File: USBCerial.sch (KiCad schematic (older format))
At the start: 3 parts, among them J1 USB_C, U1 CH340C

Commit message: First schematic complete using the CH340C
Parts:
- removed C1: 0.1uF, Capacitor_SMD:C_0603_1608Metric, symbol Device:C
- added C1, C2: 0.1uF 50V, Capacitor_SMD:C_0603_1608Metric_Pad1.08x0.95mm_HandSolder, symbol Device:C_Small
- added C3, C4: 1uF 50V, Capacitor_SMD:C_0603_1608Metric_Pad1.08x0.95mm_HandSolder, symbol Device:C_Small
- added JP1: Jumper, Connector_PinHeader_2.54mm:PinHeader_1x03_P2.54mm_Vertical, symbol Jumper:Jumper_3_Bridged12
- added U2: XC6206P332MR, Package_TO_SOT_SMD:SOT-23, symbol Regulator_Linear:XC6206PxxxMR
- U1: symbol Interface_USB:CH340C -> USBCerial:CH340C
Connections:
- net labels added: +3.3V, CTS, DTR, GNDD, RTS, RXD, TXD, VCC
- net labels removed: GND
- wire segments 12 -> 47
- no-connect marks 0 -> 6

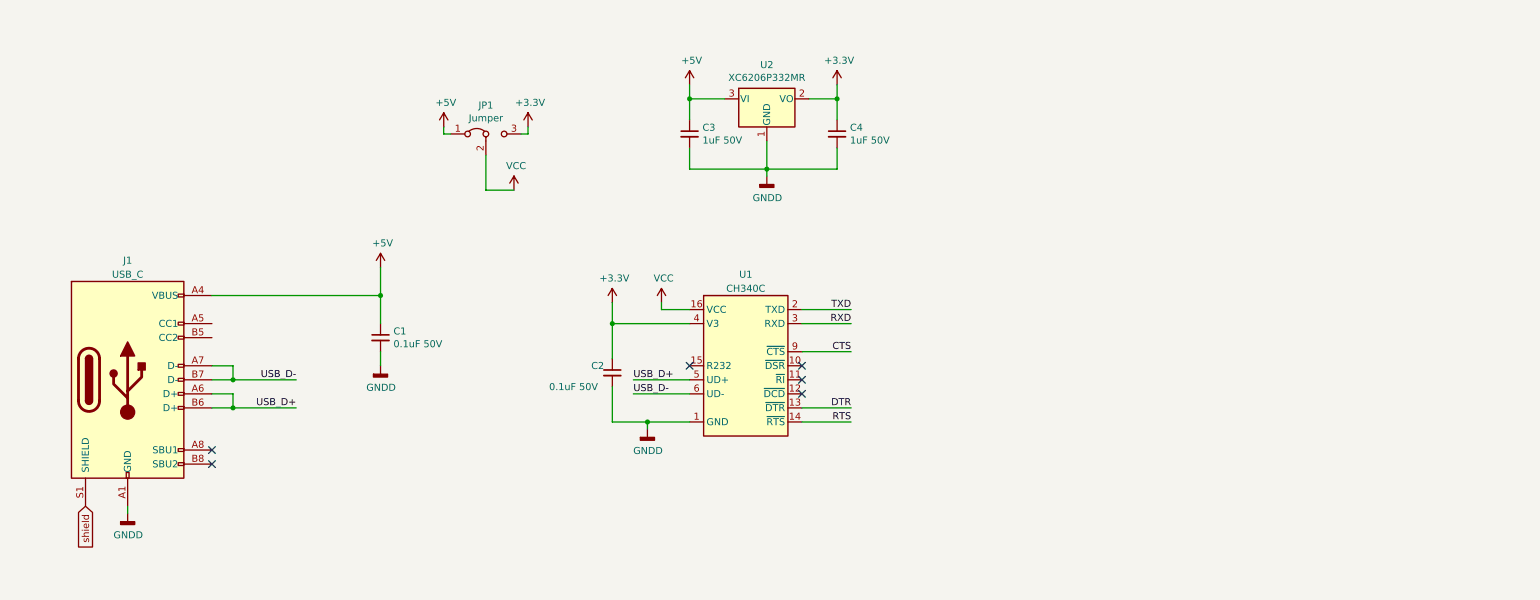
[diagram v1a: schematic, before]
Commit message: Complete schematic, Begin on PCB placment and design
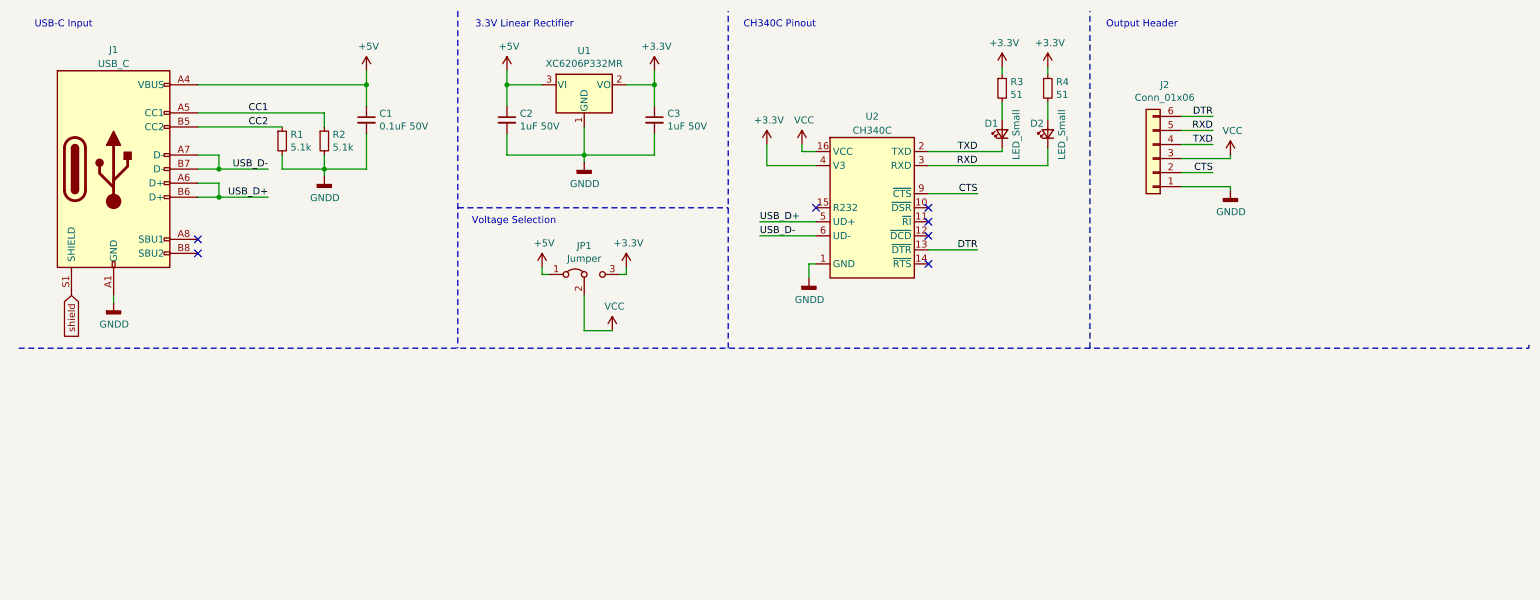
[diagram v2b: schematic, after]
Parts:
- removed C2: 0.1uF 50V, Capacitor_SMD:C_0603_1608Metric_Pad1.08x0.95mm_HandSolder, symbol Device:C_Small
- added D1, D2: LED_Small, LED_SMD:LED_0603_1608Metric_Castellated, symbol Device:LED_Small
- added J2: Conn_01x06, Connector_PinHeader_2.54mm:PinHeader_1x06_P2.54mm_Horizontal, symbol Connector_Generic:Conn_01x06
- added R1, R2: 5.1k, Resistor_SMD:R_0603_1608Metric_Pad0.98x0.95mm_HandSolder, symbol Device:R_Small
- added R3, R4: 51, Resistor_SMD:R_0603_1608Metric_Pad0.98x0.95mm_HandSolder, symbol Device:R_Small
- renumbered C3 to C2, C4 to C3, U2 to U1, U1 to U2
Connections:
- net +3V3: now also R3.1, R4.1
- net CTS: now also J2.2 (Pin_2)
- net DTR: now also J2.6 (Pin_6)
- net GNDD: now also J2.1 (Pin_1), R1.2, R2.2
- net RXD: now also D2.1 (K), J2.5 (Pin_5)
- net TXD: now also D1.1 (K), J2.4 (Pin_4)
- net VCC: now also J2.3 (Pin_3)
- net CC1: now reaches J1.A5 (CC1)
- net CC1: now also R2.1
- net CC2: now reaches J1.B5 (CC2)
- net CC2: now also R1.1
- net RTS: no longer names the net of U2.14 (~RTS)
- new net: D1.2 (A), R3.2
- new net: D2.2 (A), R4.2
- no-connect marks 6 -> 7
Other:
- note added: "3.3V Linear Rectifier"
- note added: "CH340C Pinout"
- note added: "Output Header"
- note added: "USB-C Input"
- note added: "Voltage Selection"
- moved on the sheet: C1, C2, C3, J1, JP1, U1, U2
